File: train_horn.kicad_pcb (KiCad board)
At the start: 2 copper layers, 33 x 100 mm, 104 parts, among them J1 USB_OTG, J2 PROG, Q1 2N7002, SW1 PLAY, U1 MIC7221, U2 MCP73831, U3 TPS78233DDCR, U4 MSP430FR2000_TSSOP, U5 TPA6211A1

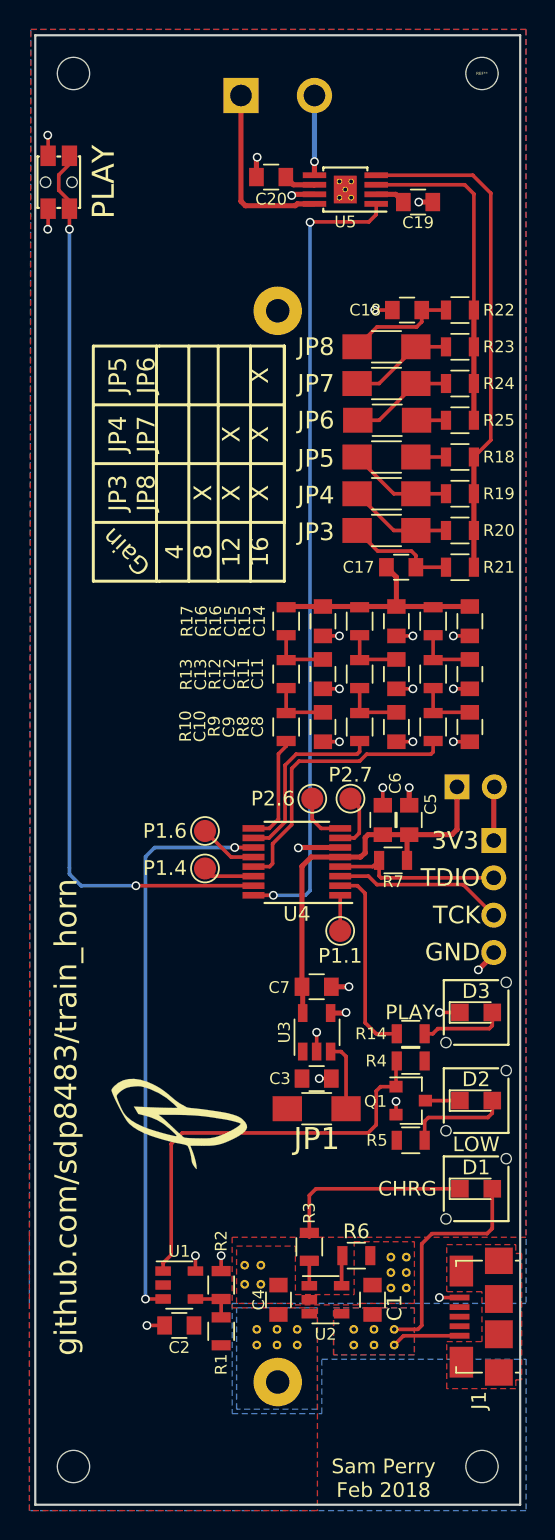
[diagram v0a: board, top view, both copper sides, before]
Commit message: add TH tact switch in place of microSMD switch, retained SMD switch as option
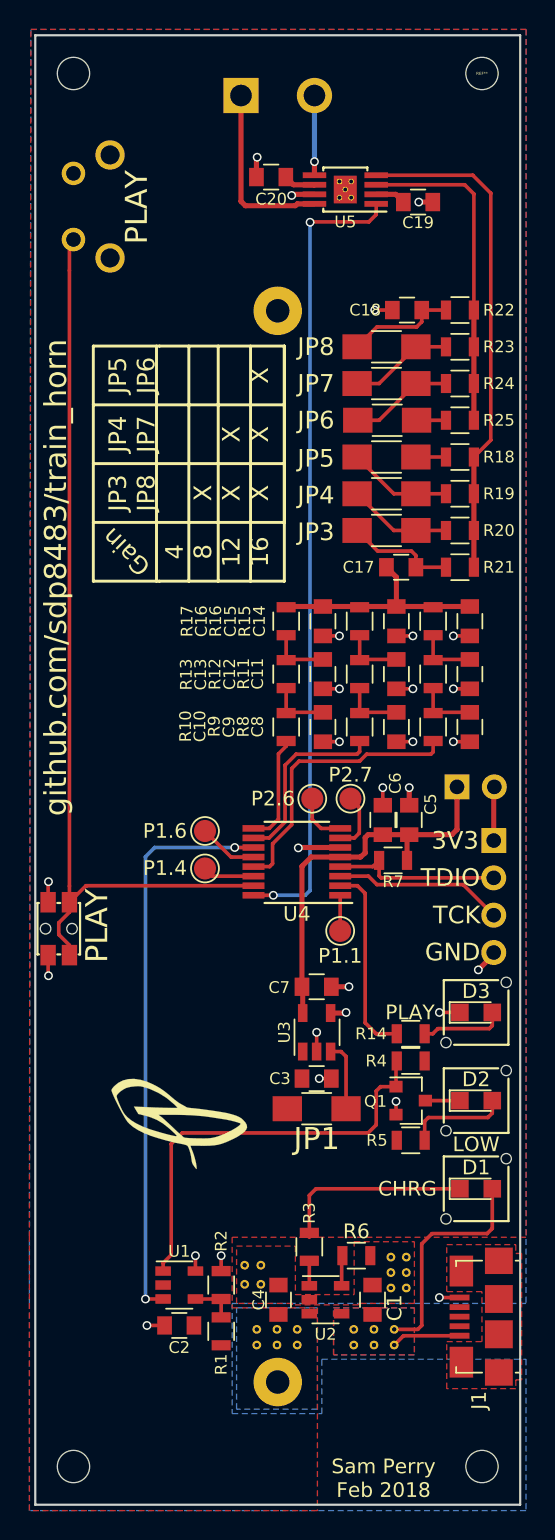
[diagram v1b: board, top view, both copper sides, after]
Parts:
- added REF**: SwitchTactile_TE_1825027-8_SPST_RightAngle_TH, lib_fp:SwitchTactile_TE_1825027-8_SPST_RightAngle_TH, B.Cu at (213.8, 74.5)
- moved SW1 50.8 mm to (212.8, 121.4)
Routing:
- net PLAY: track 62.4 -> 62.8 mm, vias 2 -> 0
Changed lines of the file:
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@@
 (kicad_pcb (version 4) (host pcbnew 4.0.7)
   (general
-    (links 158)
+    (links 160)
     (no_connects 0)
-    (area 210.274999 60.074999 245.675001 161.000001)
+    (area 211.124999 60.524999 244.275001 160.675001)
     (thickness 1.6)
-    (drawings 51)
-    (tracks 298)
+    (drawings 52)
+    (tracks 297)
     (zones 0)
-    (modules 104)
+    (modules 105)
     (nets 53)
   )
@@
     (mod_text_size 1 1)
     (mod_text_width 0.15)
-    (pad_size 1.06 0.65)
-    (pad_drill 0)
+    (pad_size 1.6 1.6)
+    (pad_drill 1)
     (pad_to_mask_clearance 0.2)
     (aux_axis_origin 0 0)
@@
     (uvia_drill 0.1)
   )
+  (module lib_fp:SwitchTactile_TE_1825027-8_SPST_RightAngle_TH (layer B.Cu)
+    (at 213.8 74.5 90)
+    (fp_text reference REF** (at 2.25 2.4 90) (layer B.SilkS) hide
+      (effects (font (size 1 1) (thickness 0.15)) (justify mirror))
+    )
+    (fp_text value SwitchTactile_TE_1825027-8_SPST_RightAngle_TH (at 2.25 1.1 90) (layer B.Fab)
+      (effects (font (size 0.5 0.5) (thickness 0.125)) (justify mirror))
+    )
+    (fp_line (start -1.5 -6) (end 6 -6) (layer B.CrtYd) (width 0.15))
+    (fp_line (start 6 -6) (end 6 4.01) (layer B.CrtYd) (width 0.15))
+    (fp_line (start 6 4.01) (end -1.5 4.01) (layer B.CrtYd) (width 0.15))
+    (fp_line (start -1.5 -6) (end -1.5 4.01) (layer B.CrtYd) (width 0.15))
+    (fp_line (start 0.495 -2.6) (end 0.495 -5.85) (layer B.Fab) (width 0.15))
+    (fp_line (start 0.495 -5.85) (end 4.005 -5.85) (layer B.Fab) (width 0.15))
+    (fp_line (start 4.005 -5.85) (end 4.005 -2.6) (layer B.Fab) (width 0.15))
+    (fp_line (start -1.31 -2.6) (end -1.31 1.08) (layer B.Fab) (width 0.15))
+    (fp_line (start -1.31 1.08) (end 5.81 1.08) (layer B.Fab) (width 0.15))
+    (fp_line (start 5.81 1.08) (end 5.81 -2.6) (layer B.SilkS) (width 0.15))
+    (fp_line (start -1.31 -2.6) (end 5.81 -2.6) (layer B.Fab) (width 0.15))
+    (fp_line (start -1.31 -2.6) (end -1.31 1.08) (layer B.SilkS) (width 0.15))
+    (fp_line (start 5.81 1.08) (end 5.81 -2.6) (layer B.Fab) (width 0.15))
+    (fp_line (start -1.31 1.08) (end 5.81 1.08) (layer B.SilkS) (width 0.15))
+    (fp_line (start -1.31 -2.6) (end 5.81 -2.6) (layer B.SilkS) (width 0.15))
+    (pad 4 thru_hole circle (at 5.755 2.49 90) (size 2 2) (drill 1.3) (layers *.Cu *.Mask))
+    (pad 1 thru_hole circle (at 0 0 90) (size 1.6 1.6) (drill 1) (layers *.Cu *.Mask)
+      (net 41 PLAY))
+    (pad 2 thru_hole circle (at 4.5 0 90) (size 1.6 1.6) (drill 1) (layers *.Cu *.Mask)
+      (net 2 GND))
+    (pad 3 thru_hole circle (at -1.255 2.49 90) (size 2 2) (drill 1.3) (layers *.Cu *.Mask))
+    (model ${KIPRJMOD}/3d_models/C-1825027-8.wrl
+      (at (xyz 0 0 0))
+      (scale (xyz 1 1 1))
+      (rotate (xyz 0 0 0))
+    )
+  )
   (module lib_fp:TerminalBlock_02x5mm_Straight (layer B.Cu)
     (at 225.2 64.7)
@@
   )
   (module SWITCH_Panasonic_SMDRight_EVQP7C (layer F.Cu)
-    (at 212.8 70.6 270)
+    (at 212.8 121.4 270)
     (fp_text reference SW1 (at 0 0 270) (layer F.SilkS) hide
       (effects (font (size 0.5 0.5) (thickness 0.125)))
@@
       (xy 2.12329 -4.558571) (xy 2.25791 -4.604433) (xy 2.314409 -4.614333) (xy 2.385564 -4.586255)) (layer F.SilkS) (width 0.01))
   )
+  (gr_text PLAY (at 215.4 121.2 90) (layer F.SilkS)
+    (effects (font (size 1.5 1.5) (thickness 0.3)))
+  )
   (gr_text "Sam Perry\nFeb 2018" (at 234.9 158.8) (layer F.SilkS)
     (effects (font (size 1 1) (thickness 0.25)))
@@
     (effects (font (size 1.5 1.5) (thickness 0.3)) (justify mirror))
   )
-  (gr_text github.com/sdp8483/train_horn (at 213.3 134.225 90) (layer F.SilkS)
+  (gr_text github.com/sdp8483/train_horn (at 212.6 97.5 90) (layer F.SilkS)
     (effects (font (size 1.5 1.5) (thickness 0.3)))
   )
@@
     (effects (font (size 1.5 1.5) (thickness 0.3)) (justify mirror))
   )
-  (gr_text PLAY (at 215.85 70.575 90) (layer F.SilkS)
+  (gr_text PLAY (at 218.1 72.3 90) (layer F.SilkS)
     (effects (font (size 1.5 1.5) (thickness 0.3)))
   )
@@
   (segment (start 226.258334 149.75) (end 226.275 149.733334) (width 0.25) (layer F.Cu) (net 1) (status 30))
   (segment (start 227.7 147.7) (end 227.75 147.65) (width 0.25) (layer F.Cu) (net 1) (status 30))
+  (segment (start 212.075 123.2) (end 212.075 124.575) (width 0.25) (layer F.Cu) (net 2))
+  (via (at 212.1 124.6) (size 0.6) (drill 0.4) (layers F.Cu B.Cu) (net 2))
+  (segment (start 212.075 124.575) (end 212.1 124.6) (width 0.25) (layer F.Cu) (net 2))
+  (segment (start 212.075 119.6) (end 212.075 118.225) (width 0.25) (layer F.Cu) (net 2))
+  (via (at 212.1 118.2) (size 0.6) (drill 0.4) (layers F.Cu B.Cu) (net 2))
+  (segment (start 212.075 118.225) (end 212.1 118.2) (width 0.25) (layer F.Cu) (net 2))
   (segment (start 231.95 115.875) (end 229.125 115.875) (width 0.35) (layer F.Cu) (net 2))
   (via (at 229.1 115.9) (size 0.6) (drill 0.4) (layers F.Cu B.Cu) (net 2))
@@
   (via (at 228.65 71.5) (size 0.6) (drill 0.4) (layers F.Cu B.Cu) (net 2))
   (segment (start 228.725 71.425) (end 228.65 71.5) (width 0.35) (layer F.Cu) (net 2))
-  (segment (start 212.075 72.4) (end 212.075 73.775) (width 0.25) (layer F.Cu) (net 2) (status 10))
-  (via (at 212.05 73.8) (size 0.6) (drill 0.4) (layers F.Cu B.Cu) (net 2))
-  (segment (start 212.075 73.775) (end 212.05 73.8) (width 0.25) (layer F.Cu) (net 2))
-  (segment (start 212.075 68.8) (end 212.075 67.425) (width 0.25) (layer F.Cu) (net 2) (status 10))
-  (via (at 212.05 67.4) (size 0.6) (drill 0.4) (layers F.Cu B.Cu) (net 2))
-  (segment (start 212.075 67.425) (end 212.05 67.4) (width 0.25) (layer F.Cu) (net 2))
   (segment (start 240.1 127.1) (end 238.7 127.1) (width 0.25) (layer F.Cu) (net 2) (status 10))
   (via (at 238.7 127.1) (size 0.6) (drill 0.4) (layers F.Cu B.Cu) (net 2))
@@
   (segment (start 240.425 70.775) (end 234.4 70.775) (width 0.25) (layer F.Cu) (net 40) (status 20))
   (segment (start 241.05 71.4) (end 240.425 70.775) (width 0.25) (layer F.Cu) (net 40))
-  (segment (start 213.525 117.25) (end 213.525 117.675) (width 0.25) (layer B.Cu) (net 41))
-  (segment (start 218.05 118.475) (end 218.025 118.475) (width 0.25) (layer F.Cu) (net 41))
-  (via (at 218.05 118.475) (size 0.6) (drill 0.4) (layers F.Cu B.Cu) (net 41))
-  (segment (start 214.325 118.475) (end 218.05 118.475) (width 0.25) (layer B.Cu) (net 41))
-  (segment (start 213.525 117.675) (end 214.325 118.475) (width 0.25) (layer B.Cu) (net 41))
-  (segment (start 213.525 117.25) (end 213.525 73.8) (width 0.25) (layer B.Cu) (net 41))
-  (via (at 213.525 73.8) (size 0.6) (drill 0.4) (layers F.Cu B.Cu) (net 41))
-  (segment (start 213.525 73.8) (end 213.525 72.4) (width 0.25) (layer F.Cu) (net 41))
-  (segment (start 226.05 118.475) (end 218.025 118.475) (width 0.25) (layer F.Cu) (net 41) (status 10))
-  (segment (start 213.525 68.8) (end 213.525 69.375) (width 0.25) (layer F.Cu) (net 41) (status 30))
-  (segment (start 213.525 69.375) (end 212.8 70.1) (width 0.25) (layer F.Cu) (net 41) (status 10))
-  (segment (start 212.8 70.1) (end 212.8 71.15) (width 0.25) (layer F.Cu) (net 41))
-  (segment (start 212.8 71.15) (end 213.525 71.875) (width 0.25) (layer F.Cu) (net 41) (status 20))
-  (segment (start 213.525 71.875) (end 213.525 72.4) (width 0.25) (layer F.Cu) (net 41) (status 30))
+  (segment (start 213.525 76.6) (end 213.525 74.775) (width 0.25) (layer F.Cu) (net 41))
+  (segment (start 213.525 74.775) (end 213.8 74.5) (width 0.25) (layer F.Cu) (net 41))
+  (segment (start 213.525 118.5) (end 213.525 76.6) (width 0.25) (layer F.Cu) (net 41))
+  (segment (start 213.525 74.775) (end 213.8 74.5) (width 0.25) (layer F.Cu) (net 41))
+  (segment (start 213.525 119.6) (end 213.525 118.5) (width 0.25) (layer F.Cu) (net 41))
+  (segment (start 213.525 123.2) (end 213.525 122.525) (width 0.25) (layer F.Cu) (net 41))
+  (segment (start 213.525 122.525) (end 212.8 121.8) (width 0.25) (layer F.Cu) (net 41))
+  (segment (start 212.8 121.8) (end 212.8 121) (width 0.25) (layer F.Cu) (net 41))
+  (segment (start 212.8 121) (end 213.525 120.275) (width 0.25) (layer F.Cu) (net 41))
+  (segment (start 213.525 120.275) (end 213.525 119.6) (width 0.25) (layer F.Cu) (net 41))
+  (segment (start 226.05 118.475) (end 214.7 118.475) (width 0.25) (layer F.Cu) (net 41))
+  (segment (start 214.7 118.475) (end 214.65 118.475) (width 0.25) (layer F.Cu) (net 41))
+  (segment (start 214.65 118.475) (end 213.525 119.6) (width 0.25) (layer F.Cu) (net 41))
   (segment (start 231.95 121.55) (end 231.95 119.125) (width 0.25) (layer F.Cu) (net 42) (status 30))
   (segment (start 226.05 117.825) (end 223.275 117.825) (width 0.25) (layer F.Cu) (net 43) (status 30))
